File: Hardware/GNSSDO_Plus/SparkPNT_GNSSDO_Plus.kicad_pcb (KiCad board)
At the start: 4 copper layers, 151.9 x 101.6 mm, 472 parts, among them J1 SMA_Edge, J10 SMA_Edge, J2 USB_C_Receptacle, J3 SMA_Edge, J4 USB_C_Receptacle, J5 MagJack_PoE, J6 microSD, J7 Qwiic_Vertical, J8 SMA_Edge, J9 Screw_Cage_3.5mm-10, Q1 MBT3904DW1, Q2 DMG2305UX, Q3 DMG2305UX, Q4 DMG2305UX, Q5 DMG2305UX, Q6 DMG2305UX, Q7 DMG2305UX, Q8 DMG2305UX, Q9 DMG2305UX, SW1 PTH_RA_h7.5mm, SW2 PTH_RA_h7.5mm, SW3 PTH_RA_h7.5mm, SW4 DPDT_Slide_SMD_7.2x3.5mm, U1 ESP32-WROVER-IE-N16R8, U10 74LVC2T45DC, U11 AP7361C-3.3V, U12 74LVC2T45DC, U13 STP3593LF, U14 74LVC2T45DC, U15 SN74LVC1G175DCK, U16 JPS-3-1+, U17 LMV7219M5, U18 MS8607-02BA, U19 PCA9306, U2 mosaic-T, U20 LMV7219M5, U23 LMV7219M5, U24 LMV7219M5, U25 AP2112K-3.3, U26 LTC4418, U27 LTC4418, U3 CH340C, U4 KSZ8041NL/I, U5 AP7361C-3.3V, U6 REC15E-2405SZ, U7 DP5305, U8 74LVC2T45DC, U9 74LVC2T45DC

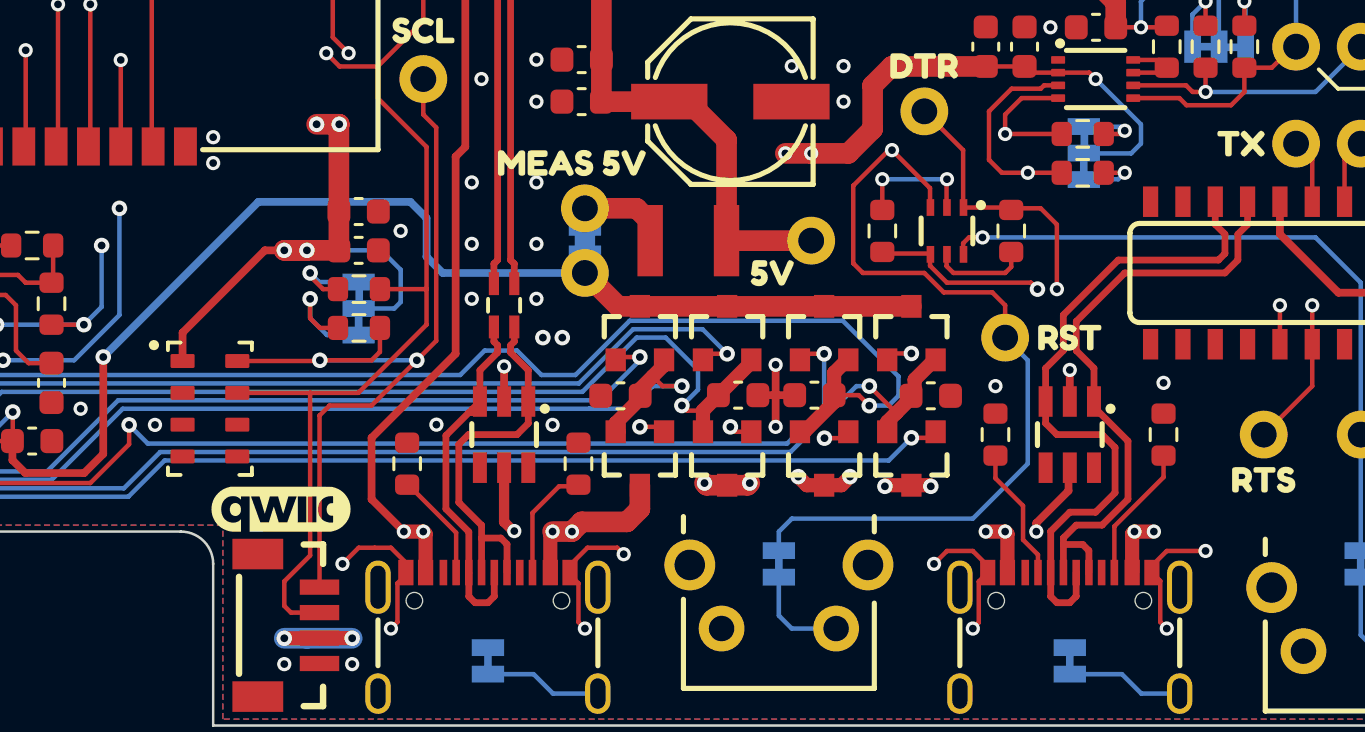
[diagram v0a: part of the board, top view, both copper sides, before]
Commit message: GNSSDO+ v02 PCB - panelized
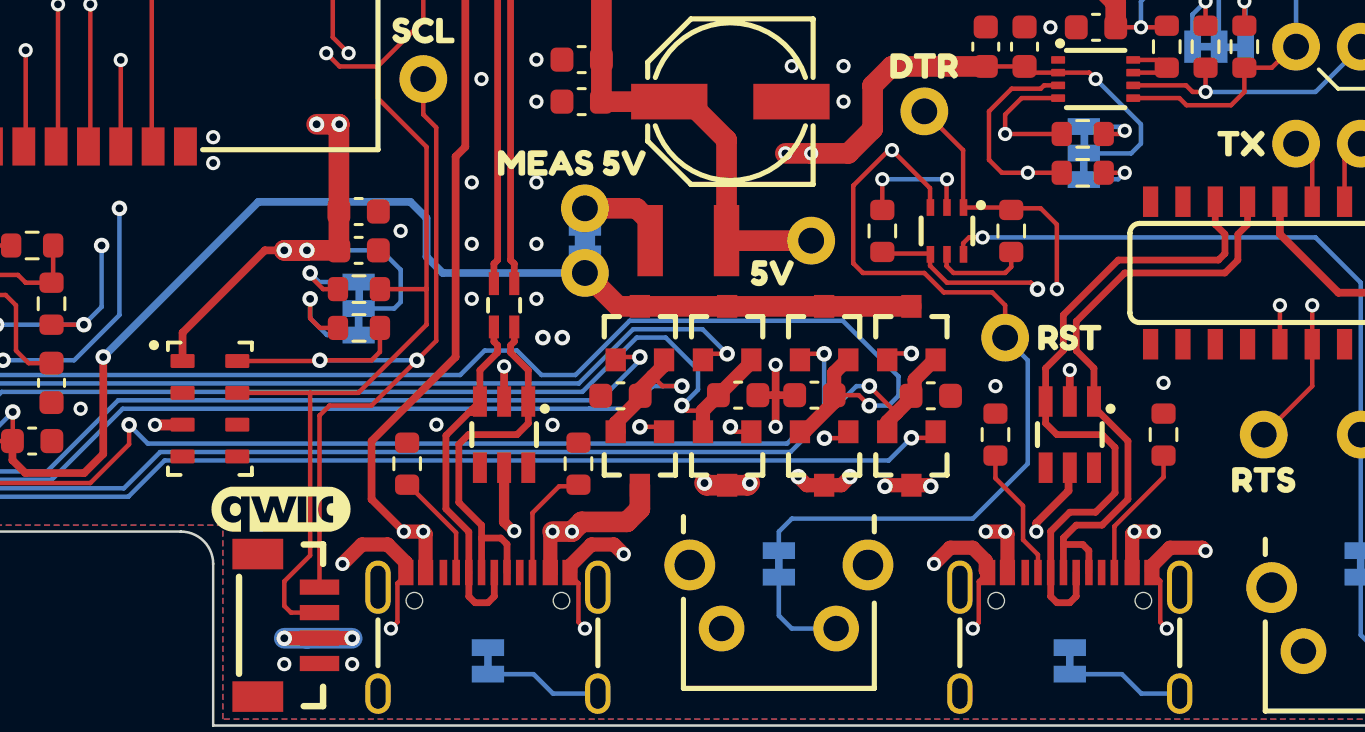
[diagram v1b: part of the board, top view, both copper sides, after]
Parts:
- moved G1 3.14 mm to (213.1, 169.4)
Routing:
- net GND: track 58.6 -> 62.4 mm
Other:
- board text removed: "P.C."
